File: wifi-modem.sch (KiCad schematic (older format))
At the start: 35 parts, among them J1 DB25_Female, J2 USB_B_Micro, U1 ESP-12E, U2 MAX3238EAIT, U3 AMS1117-3.3

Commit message: Checkpoint
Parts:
- removed U1: ESP-12E, ESP8266:ESP-12E, symbol wifi-modem-rescue:ESP-12E-ESP8266
- added R11, R12, R13, R14, R15: 10kΩ, Resistor_SMD:R_0805_2012Metric_Pad1.15x1.40mm_HandSolder, symbol Device:R_Small
- added SW1: RESET, Button_Switch_SMD:SW_Push_1P1T_NO_6x6mm_H9.5mm, symbol Switch:SW_Push
- added SW2: PROG, Button_Switch_SMD:SW_Push_1P1T_NO_6x6mm_H9.5mm, symbol Switch:SW_Push
- added U1: ESP-12F, RF_Module:ESP-12E, symbol RF_Module:ESP-12F
- J1: value DB25_Female -> RS232
- J2: value USB_B_Micro -> USB Power
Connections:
- net +3V3: now also R11.2, R12.2, R14.2, R15.2, U1.8 (VCC)
- net CD: now also R14.1, U1.17 (GPIO2)
- net CTS: now also U1.20 (GPIO5)
- net DSR: now also U1.7 (GPIO13)
- net DTR: now also U1.6 (GPIO12)
- net GND: now also R13.1, SW1.2, SW2.2, U1.15 (GND)
- net RI: now also U1.5 (GPIO14)
- net RTS: now also U1.19 (GPIO4)
- net RxD: now also U1.21 (GPIO3/RXD)
- net TxD: now also U1.22 (GPIO1/TXD)
- net at R9.1: now also U1.4 (GPIO16)
- new net: R13.2, U1.16 (GPIO15)
- new net: R15.1, SW2.1, U1.18 (GPIO0)
- new net: R11.1, U1.3 (EN)
- new net ~RST: R12.1, SW1.1, U1.1 (~RST)
- no-connect marks 35 -> 28
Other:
- moved on the sheet: C10

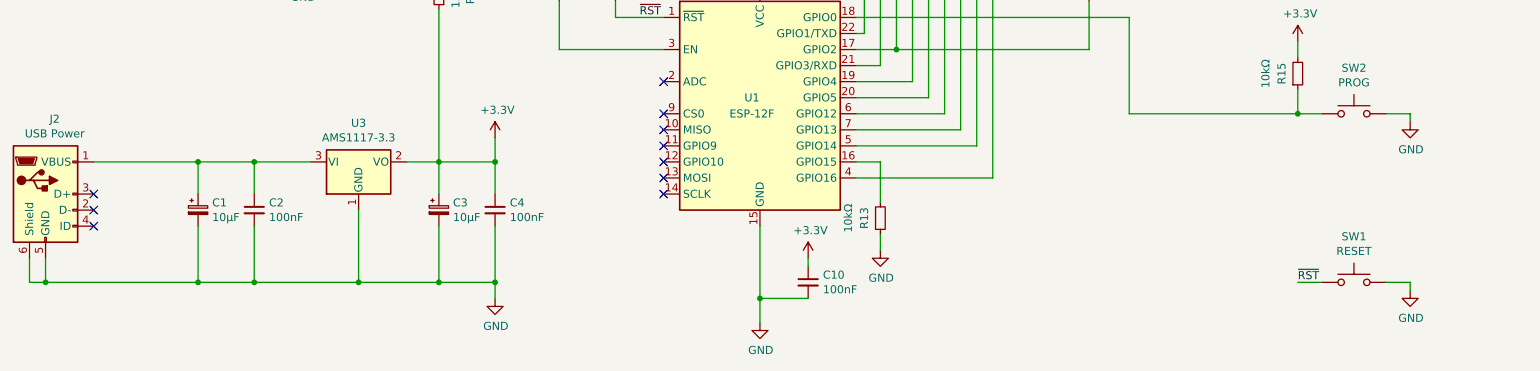
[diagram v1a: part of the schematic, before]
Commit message: Fixed connectors, added Speaker, made larger
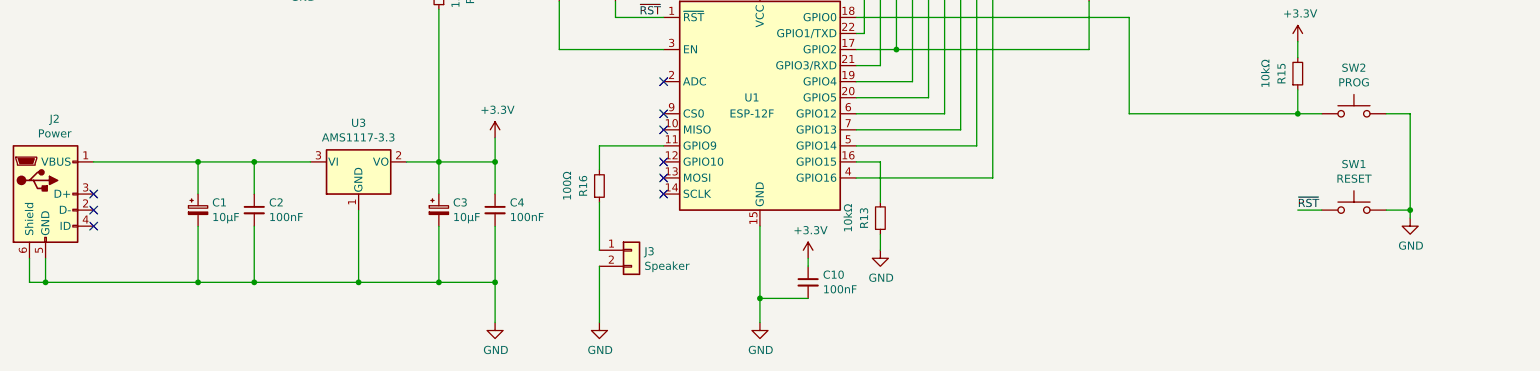
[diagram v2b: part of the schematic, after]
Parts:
- added J3: Speaker, Connector_PinHeader_2.54mm:PinHeader_1x02_P2.54mm_Vertical, symbol Connector_Generic:Conn_01x02
- added R16: 100Ω, Resistor_SMD:R_0805_2012Metric_Pad1.15x1.40mm_HandSolder, symbol Device:R_Small
- J1: footprint Connector_Dsub:DSUB-25_Female_Horizontal_P2.77x2.54mm_EdgePinOffset9.40mm -> Connector_Dsub:DSUB-25_Female_Horizontal_P2.77x2.84mm_EdgePinOffset7.70mm_Housed_MountingHolesOffset9.12mm
- J2: value USB Power -> Power; footprint Connector_USB:USB_Micro-B_Molex-105017-0001 -> Connector_USB:USB_Micro-B_Wuerth_629105150521
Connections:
- net GND: now also J3.2 (Pin_2)
- net at U1.11 (GPIO9): now also R16.2
- new net: J3.1 (Pin_1), R16.1
- no-connect marks 28 -> 27
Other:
- moved on the sheet: SW1
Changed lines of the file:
@@
 F 0 "J1" H 10550 3850 50  0000 L CNN
 F 1 "RS232" H 10550 3750 50  0000 L CNN
-F 2 "Connector_Dsub:DSUB-25_Female_Horizontal_P2.77x2.54mm_EdgePinOffset9.40mm" H 10650 2350 50  0001 C CNN
+F 2 "Connector_Dsub:DSUB-25_Female_Horizontal_P2.77x2.84mm_EdgePinOffset7.70mm_Housed_MountingHolesOffset9.12mm" H 10650 2350 50  0001 C CNN
 F 3 " ~" H 10650 2350 50  0001 C CNN
 	1    10650 2350
@@
 P 1350 5450
 F 0 "J2" H 1407 5917 50  0000 C CNN
-F 1 "USB Power" H 1407 5826 50  0000 C CNN
-F 2 "Connector_USB:USB_Micro-B_Molex-105017-0001" H 1500 5400 50  0001 C CNN
+F 1 "Power" H 1407 5826 50  0000 C CNN
+F 2 "Connector_USB:USB_Micro-B_Wuerth_629105150521" H 1500 5400 50  0001 C CNN
 F 3 "~" H 1500 5400 50  0001 C CNN
 	1    1350 5450
@@
 L power:GND #PWR0105
 U 1 1 5F51650E
-P 4150 6100
-F 0 "#PWR0105" H 4150 5850 50  0001 C CNN
-F 1 "GND" H 4155 5927 50  0000 C CNN
-F 2 "" H 4150 6100 50  0001 C CNN
-F 3 "" H 4150 6100 50  0001 C CNN
-	1    4150 6100
-	1    0    0    -1
-$EndComp
-Wire Wire Line
-	4150 6000 4150 6100
+P 4150 6250
+F 0 "#PWR0105" H 4150 6000 50  0001 C CNN
+F 1 "GND" H 4155 6077 50  0000 C CNN
+F 2 "" H 4150 6250 50  0001 C CNN
+F 3 "" H 4150 6250 50  0001 C CNN
+	1    4150 6250
+	1    0    0    -1
+$EndComp
 Connection ~ 4150 6000
 Wire Wire Line
@@
 L Switch:SW_Push SW1
 U 1 1 5F4EE562
-P 9500 6000
-F 0 "SW1" H 9500 6285 50  0000 C CNN
-F 1 "RESET" H 9500 6194 50  0000 C CNN
-F 2 "Button_Switch_SMD:SW_Push_1P1T_NO_6x6mm_H9.5mm" H 9500 6200 50  0001 C CNN
-F 3 "~" H 9500 6200 50  0001 C CNN
-	1    9500 6000
+P 9500 5550
+F 0 "SW1" H 9500 5835 50  0000 C CNN
+F 1 "RESET" H 9500 5744 50  0000 C CNN
+F 2 "Button_Switch_SMD:SW_Push_1P1T_NO_6x6mm_H9.5mm" H 9500 5750 50  0001 C CNN
+F 3 "~" H 9500 5750 50  0001 C CNN
+	1    9500 5550
 	1    0    0    -1
 $EndComp
@@
 L power:GND #PWR06
 U 1 1 5F6170C0
-P 9850 6050
-F 0 "#PWR06" H 9850 5800 50  0001 C CNN
-F 1 "GND" H 9855 5877 50  0000 C CNN
-F 2 "" H 9850 6050 50  0001 C CNN
-F 3 "" H 9850 6050 50  0001 C CNN
-	1    9850 6050
-	1    0    0    -1
-$EndComp
-Wire Wire Line
-	9700 6000 9850 6000
-Wire Wire Line
-	9850 6000 9850 6050
-Text Label 9150 6000 0    50   ~ 0
+P 9850 5600
+F 0 "#PWR06" H 9850 5350 50  0001 C CNN
+F 1 "GND" H 9855 5427 50  0000 C CNN
+F 2 "" H 9850 5600 50  0001 C CNN
+F 3 "" H 9850 5600 50  0001 C CNN
+	1    9850 5600
+	1    0    0    -1
+$EndComp
+Wire Wire Line
+	9700 5550 9850 5550
+Wire Wire Line
+	9850 5550 9850 5600
+Text Label 9150 5550 0    50   ~ 0
 ~RST
 $Comp
@@
 	1    0    0    -1
 $EndComp
-$Comp
-L power:GND #PWR0113
-U 1 1 5F82F3BD
-P 9850 5000
-F 0 "#PWR0113" H 9850 4750 50  0001 C CNN
-F 1 "GND" H 9855 4827 50  0000 C CNN
-F 2 "" H 9850 5000 50  0001 C CNN
-F 3 "" H 9850 5000 50  0001 C CNN
-	1    9850 5000
-	1    0    0    -1
-$EndComp
 Wire Wire Line
 	9700 4950 9850 4950
-Wire Wire Line
-	9850 4950 9850 5000
 $Comp
 L Device:R_Small R15
@@
 NoConn ~ 5200 4950
 NoConn ~ 5200 5050
-NoConn ~ 5200 5150
 NoConn ~ 5200 5250
 NoConn ~ 5200 5350
 NoConn ~ 5200 5450
 Wire Wire Line
-	9150 6000 9300 6000
+	9150 5550 9300 5550
+$Comp
+L power:GND #PWR01
+U 1 1 5F497A88
+P 4800 6250
+F 0 "#PWR01" H 4800 6000 50  0001 C CNN
+F 1 "GND" H 4805 6077 50  0000 C CNN
+F 2 "" H 4800 6250 50  0001 C CNN
+F 3 "" H 4800 6250 50  0001 C CNN
+	1    4800 6250
+	1    0    0    -1
+$EndComp
+$Comp
+L Device:R_Small R16
+U 1 1 5F498066
+P 4800 5400
+F 0 "R16" V 4700 5400 50  0000 C CNN
+F 1 "100Ω" V 4600 5400 50  0000 C CNN
+F 2 "Resistor_SMD:R_0805_2012Metric_Pad1.15x1.40mm_HandSolder" H 4800 5400 50  0001 C CNN
+F 3 "~" H 4800 5400 50  0001 C CNN
+	1    4800 5400
+	1    0    0    1
+$EndComp
+Wire Wire Line
+	5200 5150 4800 5150
+Wire Wire Line
+	4800 5150 4800 5300
+$Comp
+L Connector_Generic:Conn_01x02 J3
+U 1 1 5F4AE386
+P 5000 5800
+F 0 "J3" H 5080 5792 50  0000 L CNN
+F 1 "Speaker" H 5080 5701 50  0000 L CNN
+F 2 "Connector_PinHeader_2.54mm:PinHeader_1x02_P2.54mm_Vertical" H 5000 5800 50  0001 C CNN
+F 3 "~" H 5000 5800 50  0001 C CNN
+	1    5000 5800
+	1    0    0    -1
+$EndComp
+Wire Wire Line
+	4800 5500 4800 5800
+Wire Wire Line
+	4800 5900 4800 6250
+Wire Wire Line
+	4150 6000 4150 6250
+Wire Wire Line
+	9850 4950 9850 5550
+Connection ~ 9850 5550
 $EndSCHEMATC

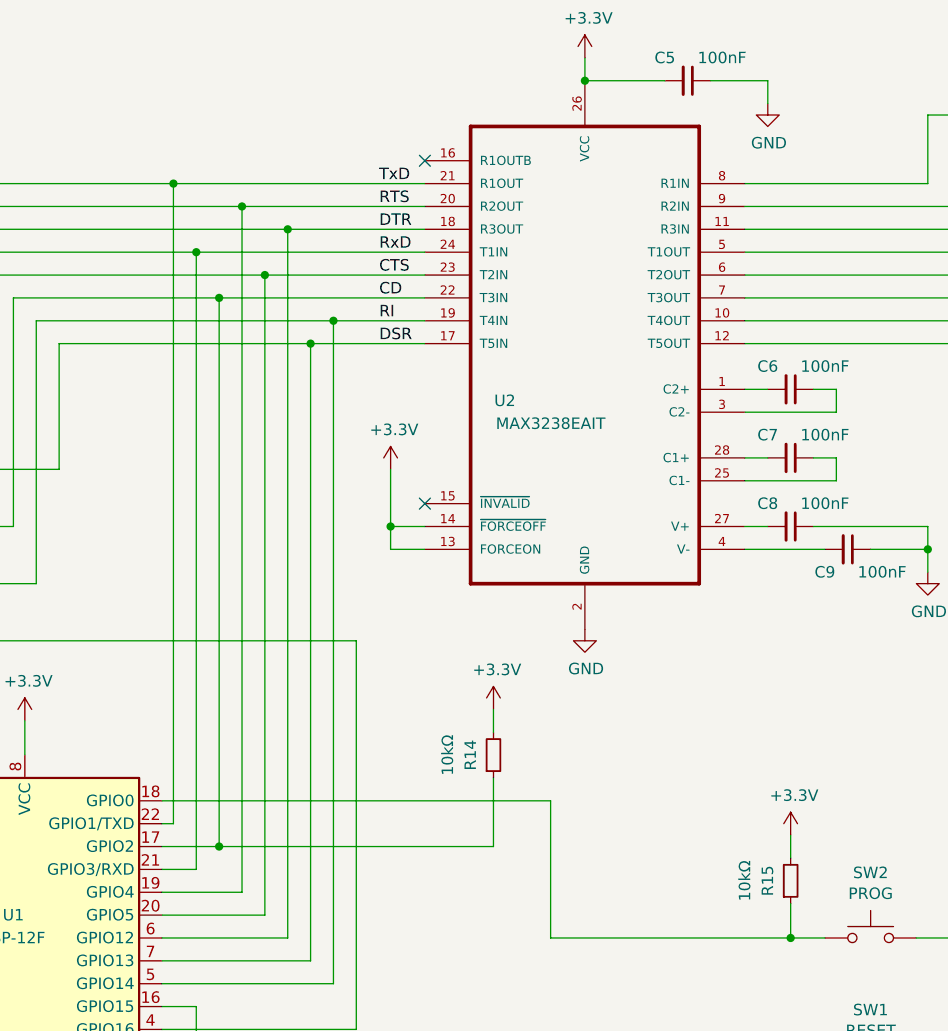
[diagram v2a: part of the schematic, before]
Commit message: Fix swapped RX/TX lines
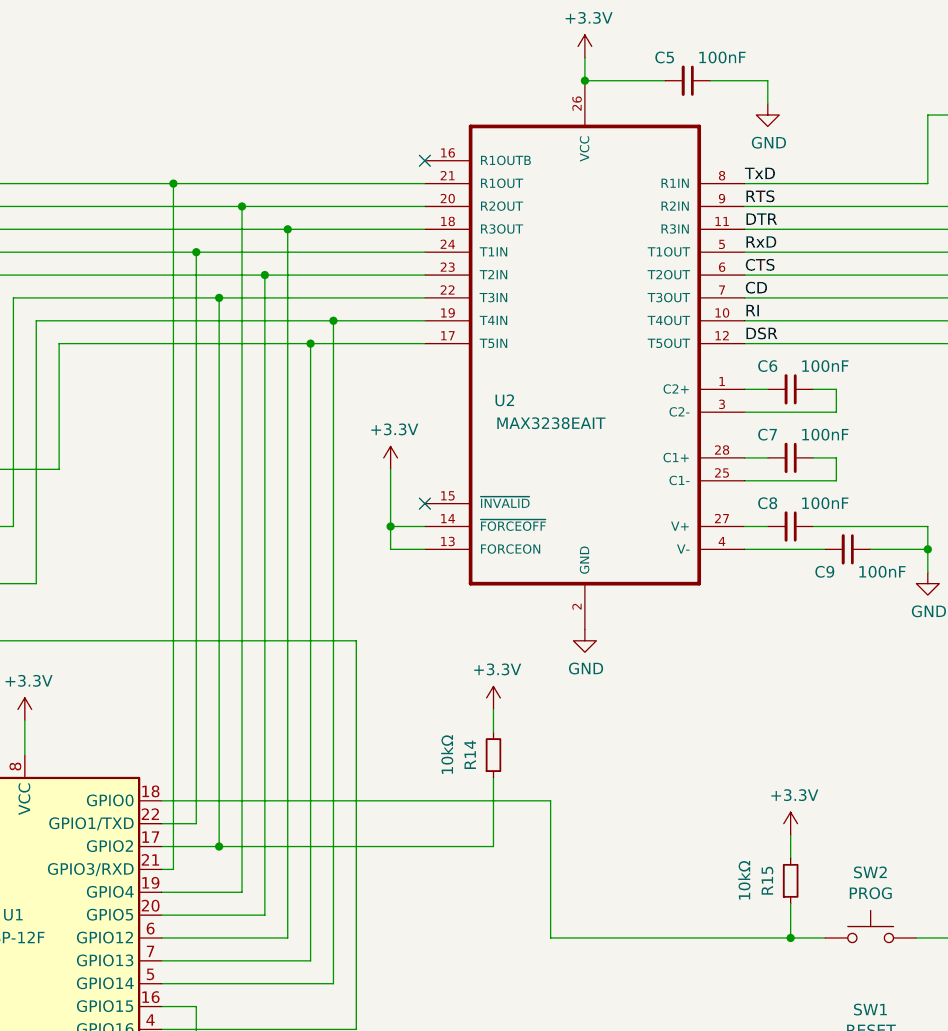
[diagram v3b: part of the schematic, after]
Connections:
- net CD: now also J1.8, U2.7 (T3OUT); no longer R14.1, R7.1, U1.17 (GPIO2), U2.22 (T3IN)
- net CTS: now also J1.5, U2.6 (T2OUT); no longer R4.1, U1.20 (GPIO5), U2.23 (T2IN)
- net DSR: now also J1.6, U2.12 (T5OUT); no longer R6.1, U1.7 (GPIO13), U2.17 (T5IN)
- net DTR: now also J1.20 (P20), U2.11 (R3IN); no longer R5.1, U1.6 (GPIO12), U2.18 (R3OUT)
- net RI: now also J1.22 (P22), U2.10 (T4OUT); no longer R8.1, U1.5 (GPIO14), U2.19 (T4IN)
- net RTS: now also J1.4, U2.9 (R2IN); no longer R3.1, U1.19 (GPIO4), U2.20 (R2OUT)
- net RxD: now also J1.3, U2.5 (T1OUT); no longer R1.1, U1.21 (GPIO3/RXD), U2.24 (T1IN)
- net TxD: now also J1.2, U2.8 (R1IN); no longer R2.1, U1.22 (GPIO1/TXD), U2.21 (R1OUT)
- new net: R6.1, U1.7 (GPIO13), U2.17 (T5IN)
- new net: R5.1, U1.6 (GPIO12), U2.18 (R3OUT)
- new net: R8.1, U1.5 (GPIO14), U2.19 (T4IN)
- new net: R3.1, U1.19 (GPIO4), U2.20 (R2OUT)
- new net: R2.1, U1.21 (GPIO3/RXD), U2.21 (R1OUT)
- new net: R14.1, R7.1, U1.17 (GPIO2), U2.22 (T3IN)
- new net: R4.1, U1.20 (GPIO5), U2.23 (T2IN)
- new net: R1.1, U1.22 (GPIO1/TXD), U2.24 (T1IN)
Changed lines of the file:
@@
 Wire Wire Line
 	5450 1750 6750 1750
-Wire Wire Line
-	5250 1950 6550 1950
-Wire Wire Line
-	5350 1650 6450 1650
 $Comp
 L Connector:DB25_Female J1
@@
 Wire Wire Line
 	10200 2350 10200 3700
-Text Label 7350 2250 0    50   ~ 0
+Text Label 8950 2250 0    50   ~ 0
 RI
-Text Label 7350 2350 0    50   ~ 0
+Text Label 8950 2350 0    50   ~ 0
 DSR
-Text Label 7350 2150 0    50   ~ 0
+Text Label 8950 2150 0    50   ~ 0
 CD
-Text Label 7350 2050 0    50   ~ 0
+Text Label 8950 2050 0    50   ~ 0
 CTS
-Text Label 7350 1950 0    50   ~ 0
+Text Label 8950 1950 0    50   ~ 0
 RxD
-Text Label 7350 1850 0    50   ~ 0
+Text Label 8950 1850 0    50   ~ 0
 DTR
-Text Label 7350 1750 0    50   ~ 0
+Text Label 8950 1750 0    50   ~ 0
 RTS
-Text Label 7350 1650 0    50   ~ 0
+Text Label 8950 1650 0    50   ~ 0
 TxD
 $Comp
@@
 ~RST
 Wire Wire Line
-	6400 4450 6450 4450
-Wire Wire Line
-	6450 4450 6450 1650
-Connection ~ 6450 1650
-Wire Wire Line
-	6450 1650 7550 1650
-Wire Wire Line
 	8100 4350 8100 4950
 Wire Wire Line
@@
 Wire Wire Line
 	7850 4550 7850 4250
-Wire Wire Line
-	6400 4650 6550 4650
-Wire Wire Line
-	6550 4650 6550 1950
-Connection ~ 6550 1950
-Wire Wire Line
-	6550 1950 7550 1950
 $Comp
 L Device:R_Small R13
@@
 	9850 4950 9850 5550
 Connection ~ 9850 5550
+Wire Wire Line
+	5350 1650 6450 1650
+Wire Wire Line
+	5250 1950 6550 1950
+Wire Wire Line
+	6400 4450 6550 4450
+Wire Wire Line
+	6550 4450 6550 1950
+Connection ~ 6550 1950
+Wire Wire Line
+	6550 1950 7550 1950
+Wire Wire Line
+	6400 4650 6450 4650
+Wire Wire Line
+	6450 4650 6450 1650
+Connection ~ 6450 1650
+Wire Wire Line
+	6450 1650 7550 1650
 $EndSCHEMATC

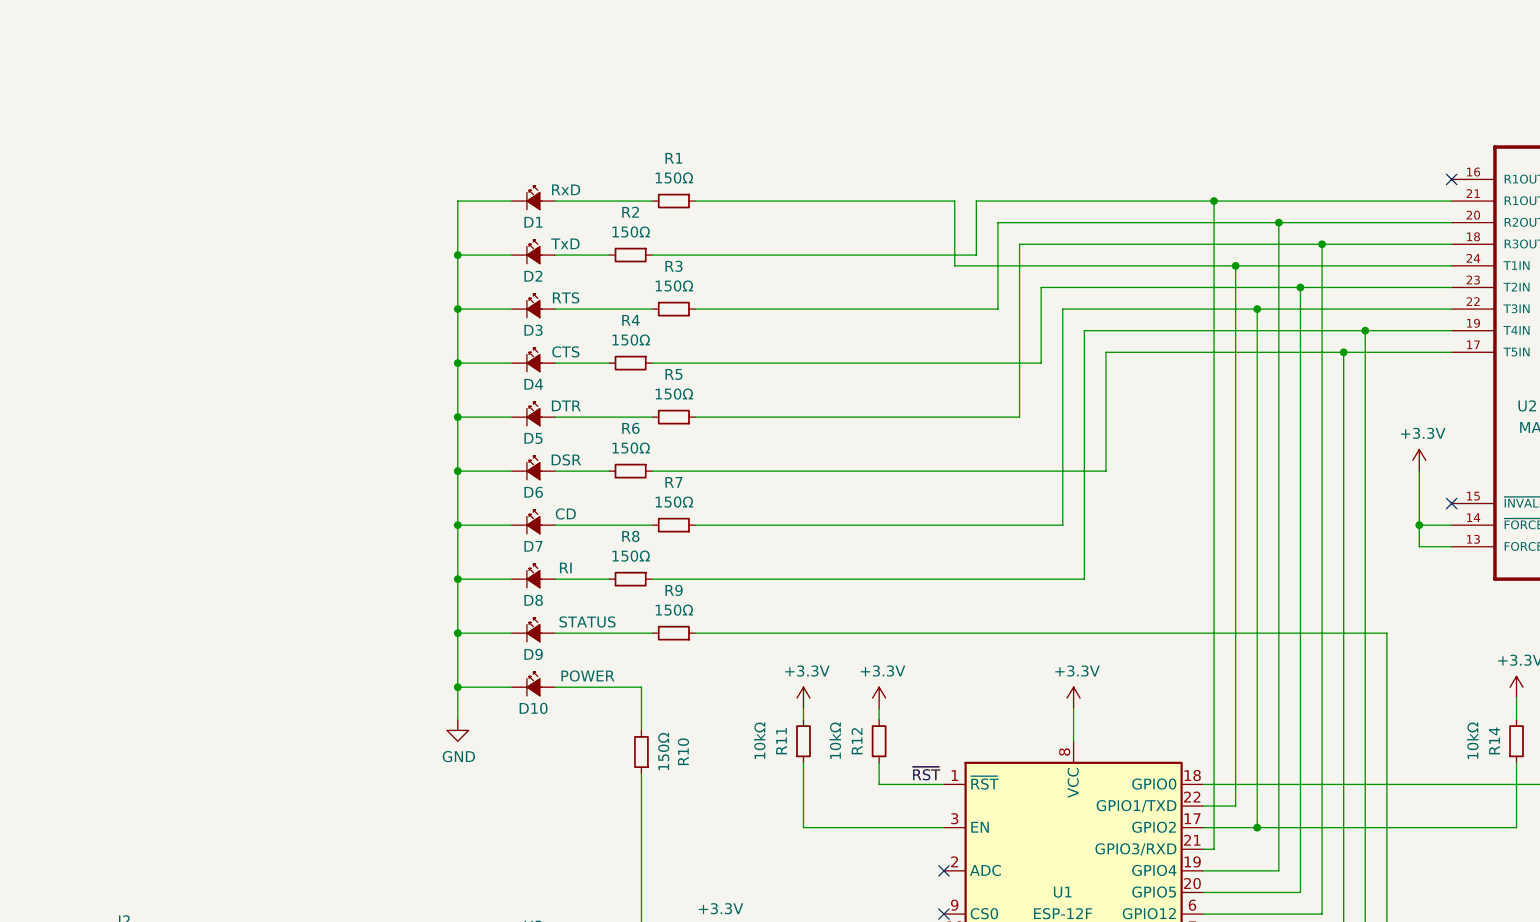
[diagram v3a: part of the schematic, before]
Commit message: Added LED drivers
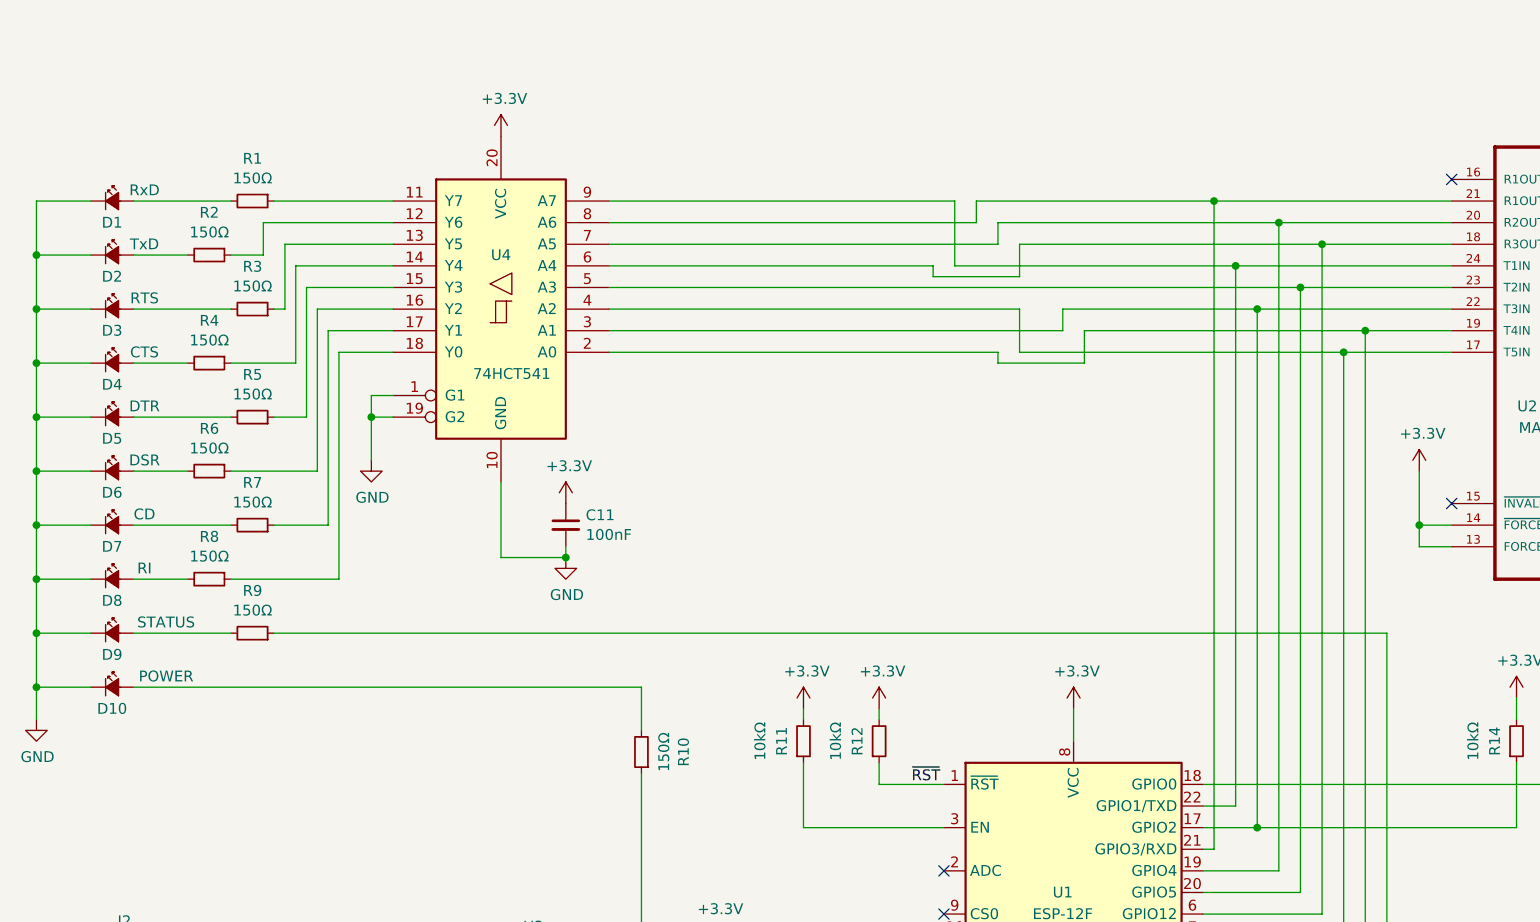
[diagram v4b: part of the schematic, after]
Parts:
- added C11: 100nF, Capacitor_SMD:C_0805_2012Metric_Pad1.15x1.40mm_HandSolder, symbol Device:C_Small
- added U4: 74HCT541, Package_SO:SSOP-20_5.3x7.2mm_P0.65mm, symbol 74xx:74HCT541
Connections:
- net +3V3: now also C11.1, U4.20 (VCC)
- net GND: now also C11.2, U4.1 (G1), U4.10 (GND), U4.19 (G2)
- net at U1.7 (GPIO13), U2.17 (T5IN): now also U4.4 (A2); no longer R6.1
- net at U1.6 (GPIO12), U2.18 (R3OUT): now also U4.6 (A4); no longer R5.1
- net at U1.5 (GPIO14), U2.19 (T4IN): now also U4.2 (A0); no longer R8.1
- net at U1.19 (GPIO4), U2.20 (R2OUT): now also U4.7 (A5); no longer R3.1
- net at U1.21 (GPIO3/RXD), U2.21 (R1OUT): now also U4.8 (A6); no longer R2.1
- net at R14.1, U1.17 (GPIO2), U2.22 (T3IN): now also U4.3 (A1); no longer R7.1
- net at U1.20 (GPIO5), U2.23 (T2IN): now also U4.5 (A3); no longer R4.1
- net at U1.22 (GPIO1/TXD), U2.24 (T1IN): now also U4.9 (A7); no longer R1.1
- new net: R1.1, U4.11 (Y7)
- new net: R2.1, U4.12 (Y6)
- new net: R3.1, U4.13 (Y5)
- new net: R4.1, U4.14 (Y4)
- new net: R5.1, U4.15 (Y3)
- new net: R6.1, U4.16 (Y2)
- new net: R7.1, U4.17 (Y1)
- new net: R8.1, U4.18 (Y0)
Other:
- moved on the sheet: D1, D10, D2, D3, D4, D5, D6, D7, D8, D9, R1, R2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
